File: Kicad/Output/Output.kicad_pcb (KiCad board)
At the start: 2 copper layers, 13 parts, among them J1 Conn_01x02, J2 Conn_01x03

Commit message: OP Filter PCB Done
OP Filter PCB finished
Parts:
- L1, L2: footprint 1422455C:1422455C -> OutputInductor:IND_HCTI-220-5.8
- moved TP1 29.4 mm to (142.0, 123.2)
- moved TP2 29.2 mm to (163.0, 123.2)
- moved L1 20.9 mm to (121.6, 101.6), turned to 0 degrees
- moved L2 11.7 mm to (184.2, 101.6), turned to 0 degrees
- moved H3 9.62 mm to (194.8, 76.3)
- moved H4 9.39 mm to (109.9, 76.4)
- moved H1 8.75 mm to (194.8, 123.0)
- moved H2 8.50 mm to (109.9, 123.2)
- moved J2 8.40 mm to (148.0, 80.8)
- moved C1 2.41 mm to (134.2, 84.8)
- moved C3 2.28 mm to (171.8, 84.8)
- moved C2 1.98 mm to (153.0, 120.0)
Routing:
- added copper zone on B.Cu, net /OutputFilter/SIG+
- added copper zone on B.Cu, net /OutputFilter/SIG-
- added copper zone on F.Cu, net /OutputFilter/SPEAKER+
- added copper zone on F.Cu, net /OutputFilter/SPEAKER-
- added copper zone on F.Cu, net GNDPWR
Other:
- board outline added: 93.7 x 58.7 mm

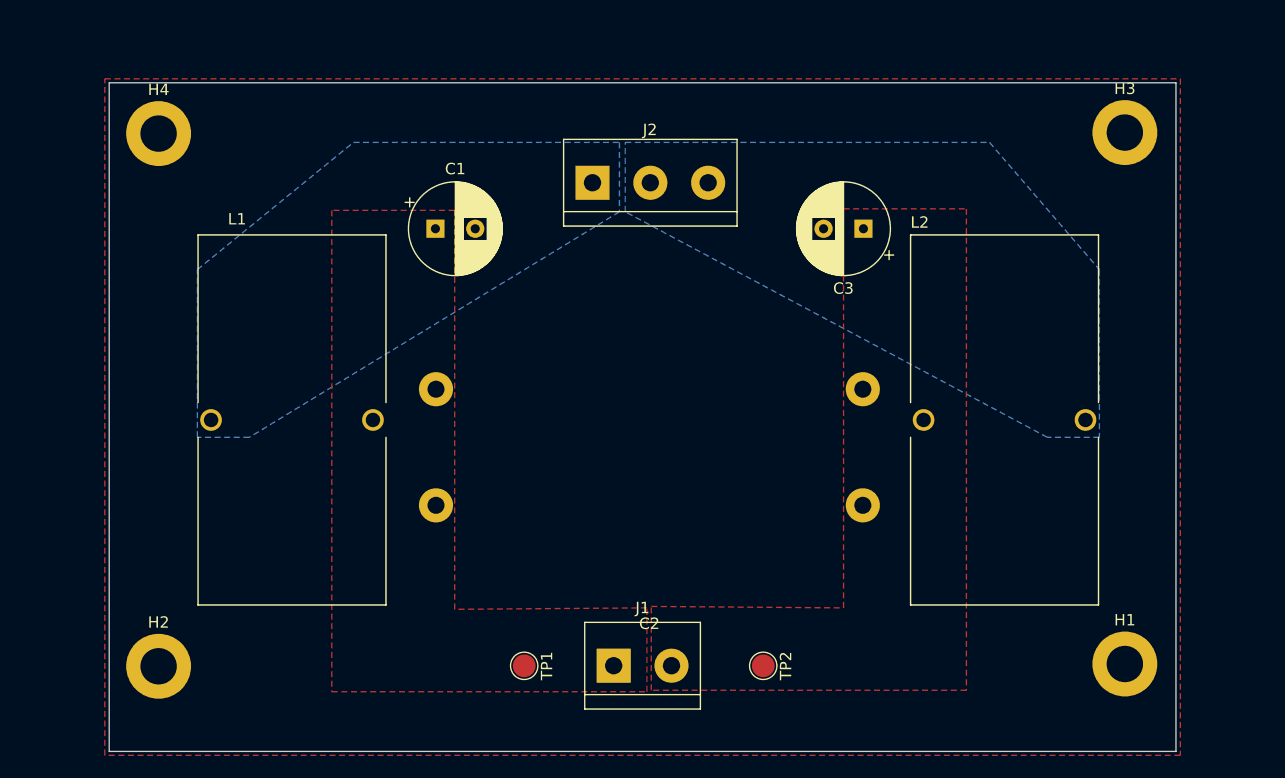
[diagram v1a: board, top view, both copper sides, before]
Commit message: Flipped J2, added connector labels
Flipped J2 and re-drew planes to connect Sig + and - respectively .
Also added labels for all the connections for J1 and J2 as well as the testpoints
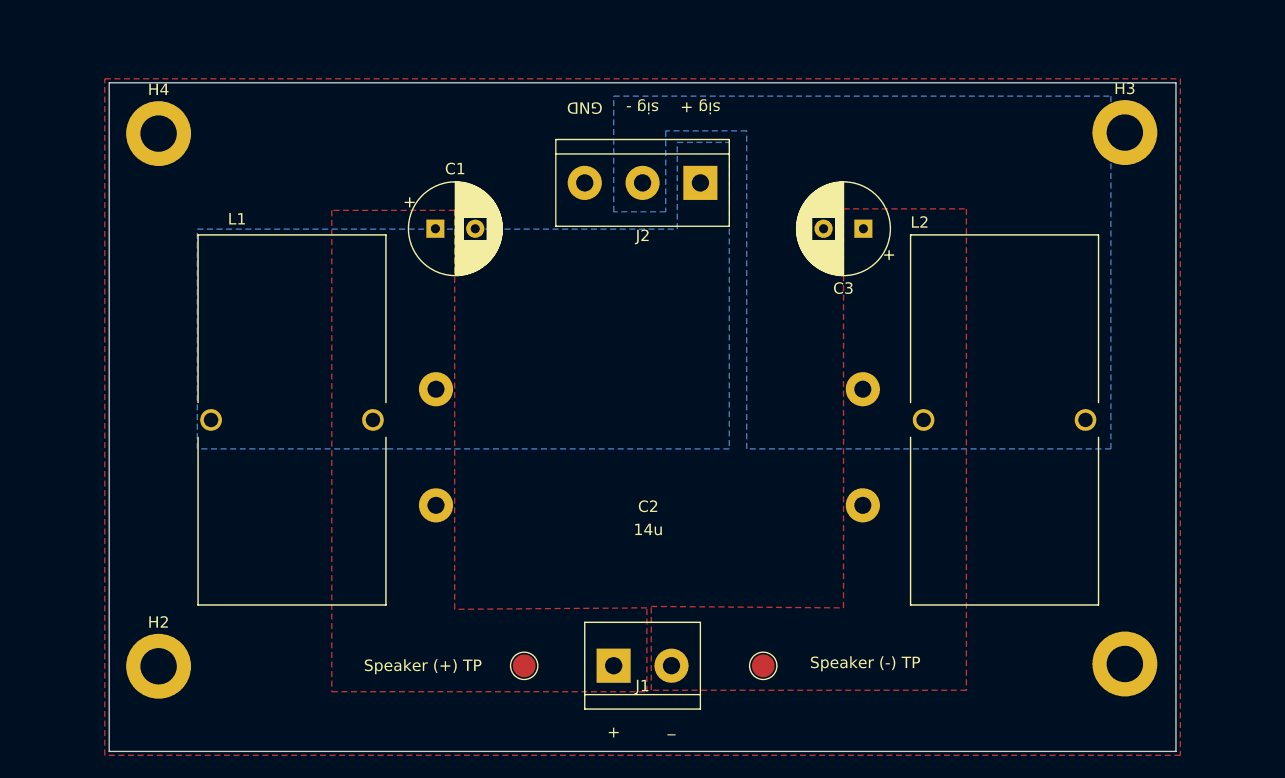
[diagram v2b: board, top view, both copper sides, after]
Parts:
- Speaker (+) TP: renamed from TP1
- Speaker (-) TP: renamed from TP2
- moved J2 9.48 mm to (157.5, 80.8), turned to 180 degrees
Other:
- board text added: "+"
- board text added: "GND"
- board text added: "_"
- board text added: "sig +"
- board text added: "sig -"

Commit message: Switched around component sides to match connector
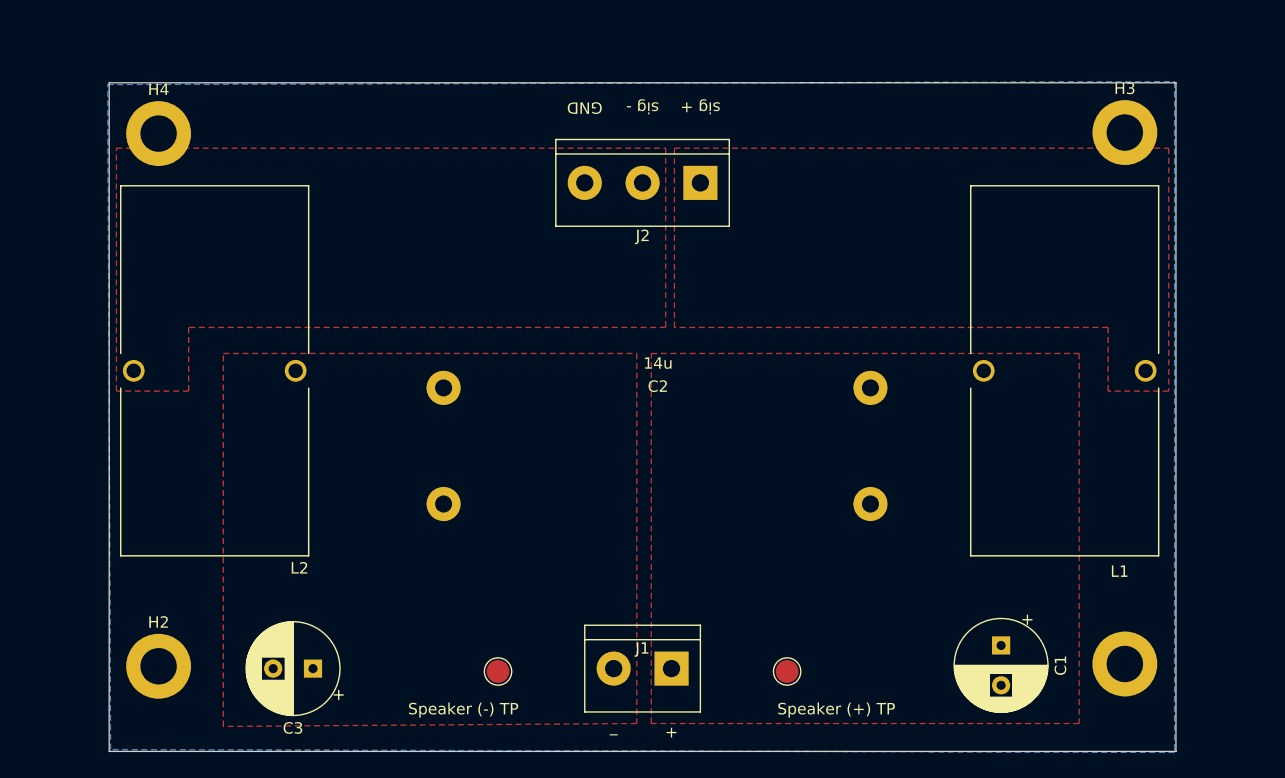
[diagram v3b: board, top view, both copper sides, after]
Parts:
- moved L2 69.5 mm to (114.8, 97.3), turned to 180 degrees
- moved L1 68.0 mm to (189.5, 97.3), turned to 180 degrees
- moved C3 61.9 mm to (123.4, 123.4)
- moved C1 61.7 mm to (183.9, 121.4), turned to 270 degrees
- moved C2 32.1 mm to (153.7, 87.9), turned to 0 degrees
- moved Speaker (-) TP 23.3 mm to (139.7, 123.7)
- moved Speaker (+) TP 23.1 mm to (165.1, 123.7)
- moved J1 5.09 mm to (154.9, 123.4), turned to 180 degrees
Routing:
- added copper zone on F.Cu, net /OutputFilter/SIG+
- added copper zone on F.Cu, net /OutputFilter/SIG-
- added copper zone on B.Cu, net GNDPWR
- removed copper zone on B.Cu, net /OutputFilter/SIG+
- removed copper zone on B.Cu, net /OutputFilter/SIG-
- removed copper zone on F.Cu, net GNDPWR

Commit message: Moved filter caps (slightly)
Shifted them such that they're as close as possible to the larger cap with enough physical clearance, and made the both symmetrical too
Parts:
- moved C3 5.39 mm to (127.3, 119.6), turned to 270 degrees
- moved C1 4.44 mm to (179.8, 119.6)
